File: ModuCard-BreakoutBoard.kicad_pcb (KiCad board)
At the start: 2 copper layers, 41 parts, among them J1 09031967921, J10 USB_C_Receptacle_USB2.0_16P, J9 RJ45_LED_Shielded, Q1 AO3401A, Q2 AO3401A, SW1 SW_SPDT_321, SW2 SW_SPDT_321, SW3 SW_SPDT_321, U1 XL4015, U2 IP4234CZ6,115

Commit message: Create fundamental layout
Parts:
- added J11: Barrel_Jack_Switch, Connector_BarrelJack:BarrelJack_Kycon_KLDX-0202-xC_Horizontal, F.Cu at (31.2, 78.5)
- added J3: Conn_01x16_Pin, Connector_PinHeader_2.54mm:PinHeader_1x16_P2.54mm_Vertical, F.Cu at (25.1, 113.0)
- added J4: Conn_01x16_Pin, Connector_PinHeader_2.54mm:PinHeader_1x16_P2.54mm_Vertical, F.Cu at (36.0, 63.9)
- added J5: Conn_01x16_Pin, Connector_PinHeader_2.54mm:PinHeader_1x16_P2.54mm_Vertical, F.Cu at (54.0, 64.0)
- added J6: Barrel_Jack_Switch, Connector_BarrelJack:BarrelJack_Kycon_KLDX-0202-xC_Horizontal, F.Cu at (30.5, 58.5)
- added J7: Conn_01x02_Pin, Connector_PinHeader_2.54mm:PinHeader_1x02_P2.54mm_Vertical, F.Cu at (52.9, 30.5)
- added J8: Conn_01x02_Pin, Connector_PinHeader_2.54mm:PinHeader_1x02_P2.54mm_Vertical, F.Cu at (52.9, 36.7)
- L1: value 4.7uH,25mA -> 40uH; footprint PCM_JLCPCB:L_1206 -> Inductor_SMD:L_Bourns_SRR1260
- moved U2 67.3 mm to (53.0, 23.0), turned to -90 degrees
- moved R9 62.3 mm to (54.8, 20.3), turned to 180 degrees
- moved J10 61.9 mm to (60.5, 23.0), turned to 90 degrees
- moved H3 61.2 mm to (70.5, 14.0)
- moved C8 60.4 mm to (57.1, 17.1), turned to 180 degrees
- moved H2 59.0 mm to (14.5, 113.0)
- moved R10 58.8 mm to (54.7, 25.6), turned to 180 degrees
- moved H4 54.6 mm to (68.5, 113.5)
- moved R8 52.4 mm to (56.9, 28.9), turned to 180 degrees
- moved C9 52.4 mm to (54.7, 26.6), turned to 180 degrees
- moved H1 42.8 mm to (14.5, 14.0)
- moved D2 41.1 mm to (22.0, 24.0), turned to 180 degrees
- moved SW2 40.3 mm to (25.2, 69.0)
- moved D5 40.1 mm to (24.0, 14.0)
- moved Q1 37.3 mm to (34.6, 60.0), turned to 180 degrees
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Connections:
- R5 pad 2: +12V_DC_JACK -> +12V
- R6 pad 2: +12V_DC_JACK -> +12V
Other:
- board outline added: 54 x 101 mm

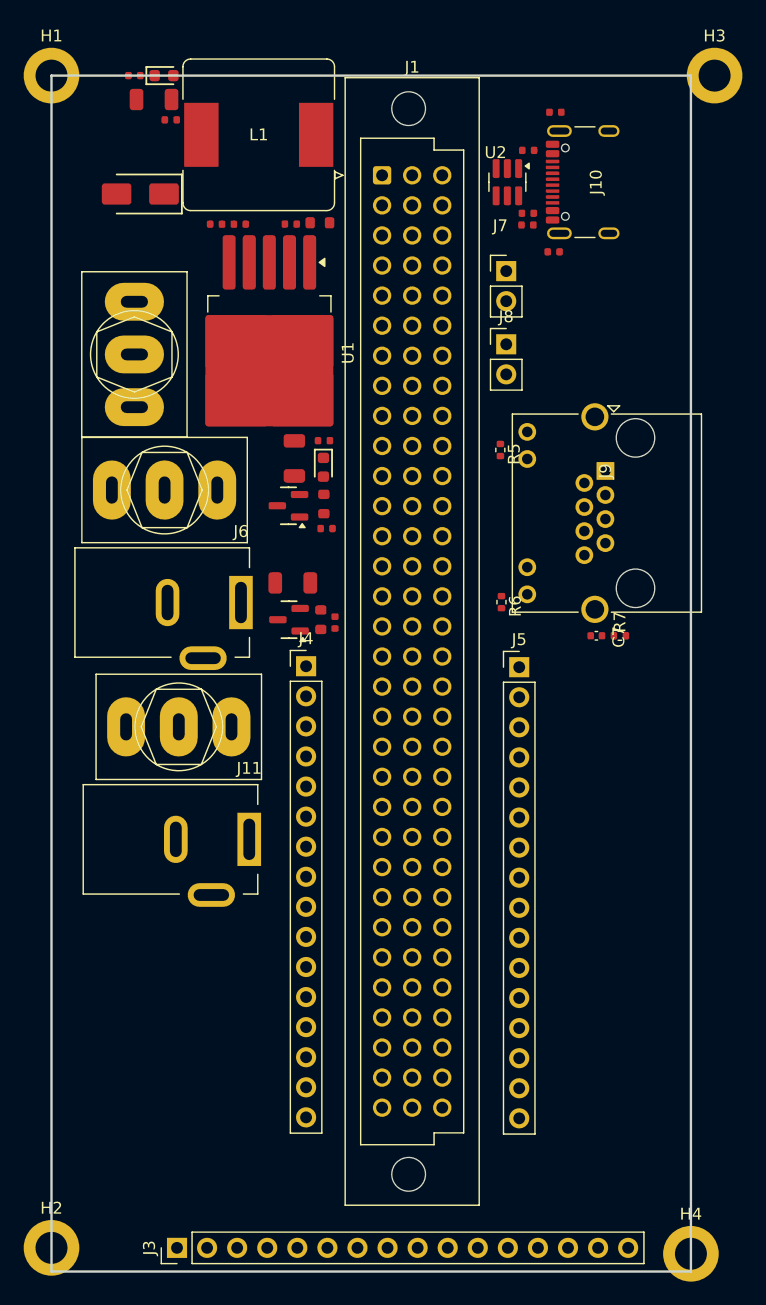
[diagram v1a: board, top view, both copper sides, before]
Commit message: Fix converter placement
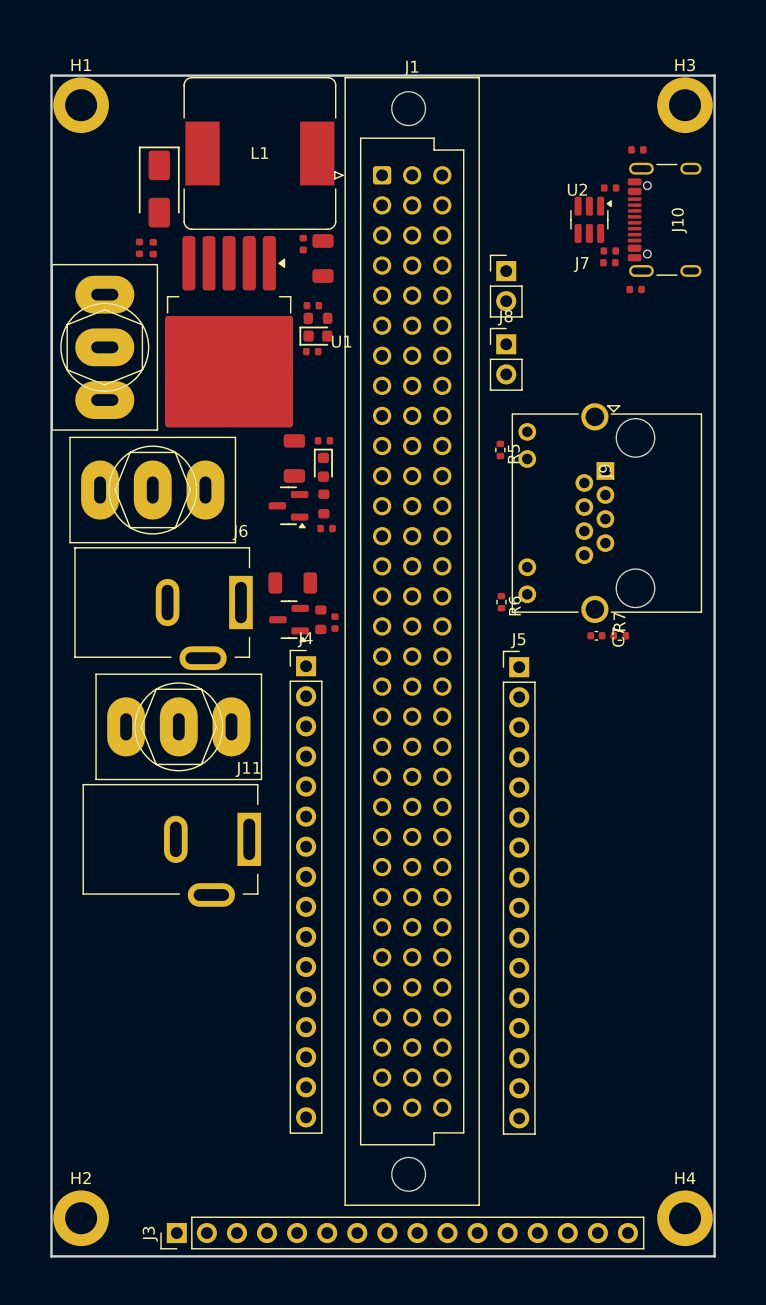
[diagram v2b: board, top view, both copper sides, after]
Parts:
- moved R4 27.7 mm to (36.5, 37.3), turned to 0 degrees
- moved D5 25.6 mm to (37.0, 36.0)
- moved C5 19.6 mm to (37.4, 29.4), turned to -90 degrees
- moved C4 15.3 mm to (35.8, 28.2), turned to -90 degrees
- moved R1 8.07 mm to (37.0, 34.5), turned to 180 degrees
- moved C8 7.62 mm to (64.0, 20.3)
- moved C9 7.62 mm to (61.6, 29.8)
- moved R10 7.62 mm to (61.6, 28.8)
- moved R8 7.62 mm to (63.8, 32.1)
- moved J10 7.62 mm to (67.4, 26.2)
- moved R9 7.62 mm to (61.7, 23.5)
- moved U2 7.62 mm to (59.9, 26.2)
- moved C1 7.58 mm to (23.1, 28.6), turned to 90 degrees
- moved R2 7.13 mm to (36.6, 33.4), turned to 0 degrees
- moved C3 6.77 mm to (21.9, 28.6), turned to 90 degrees
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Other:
- board size 54 x 101 mm -> 56 x 99.7 mm

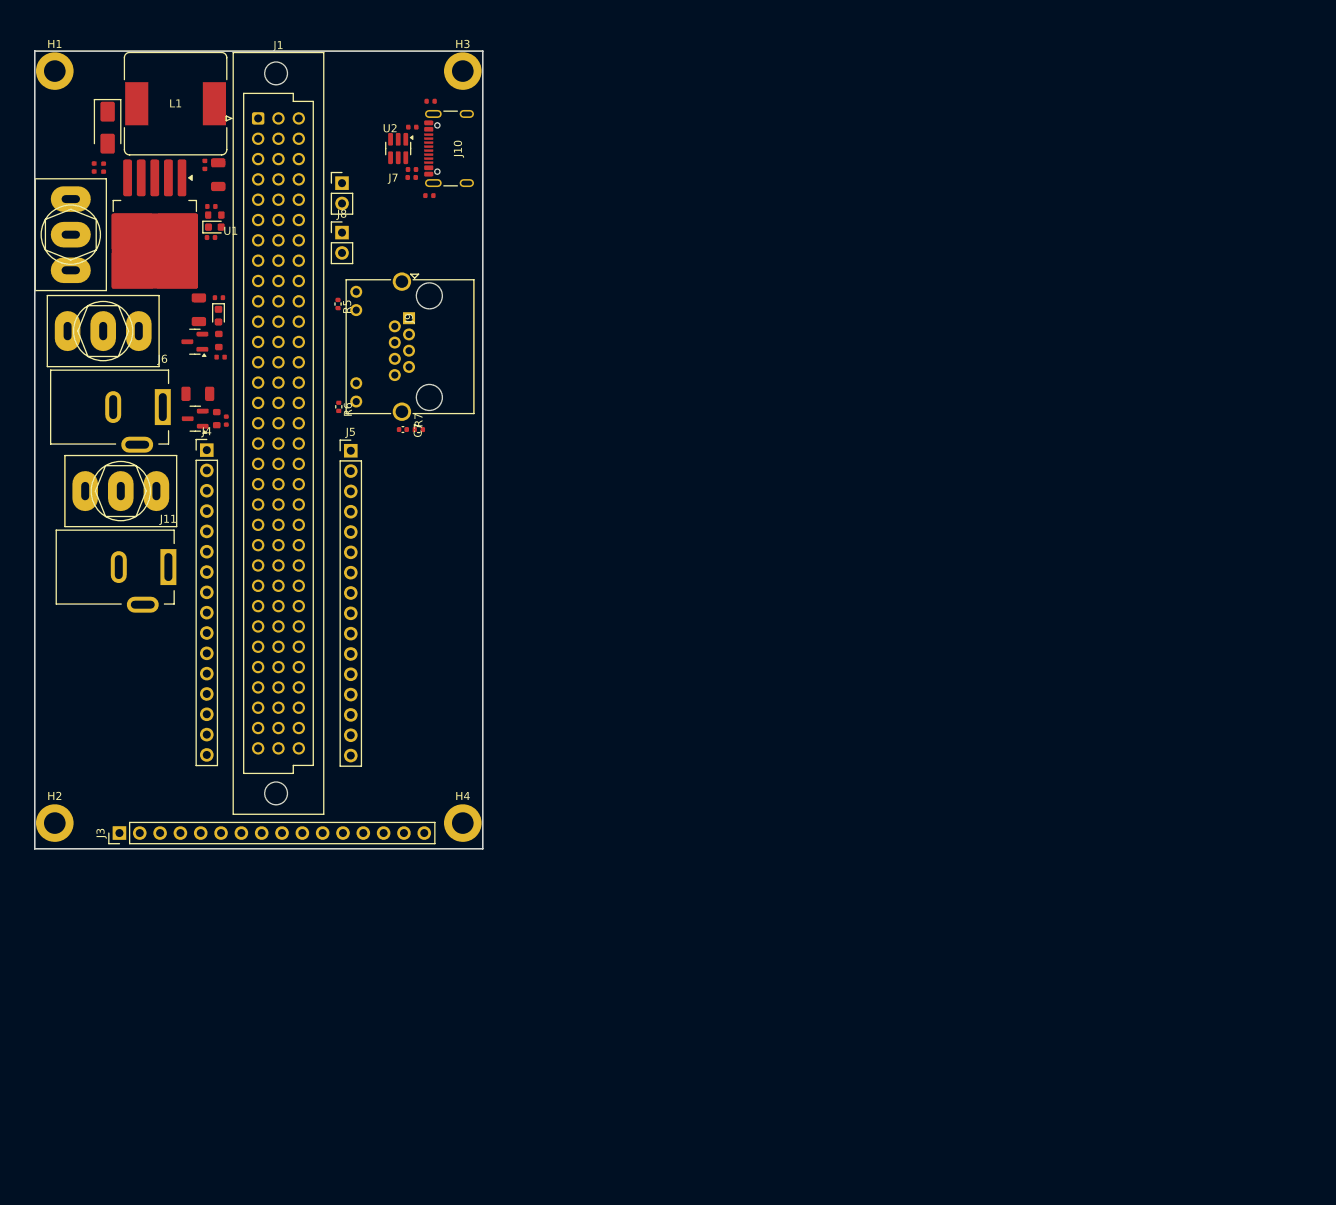
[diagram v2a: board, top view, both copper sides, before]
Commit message: Change PCB size
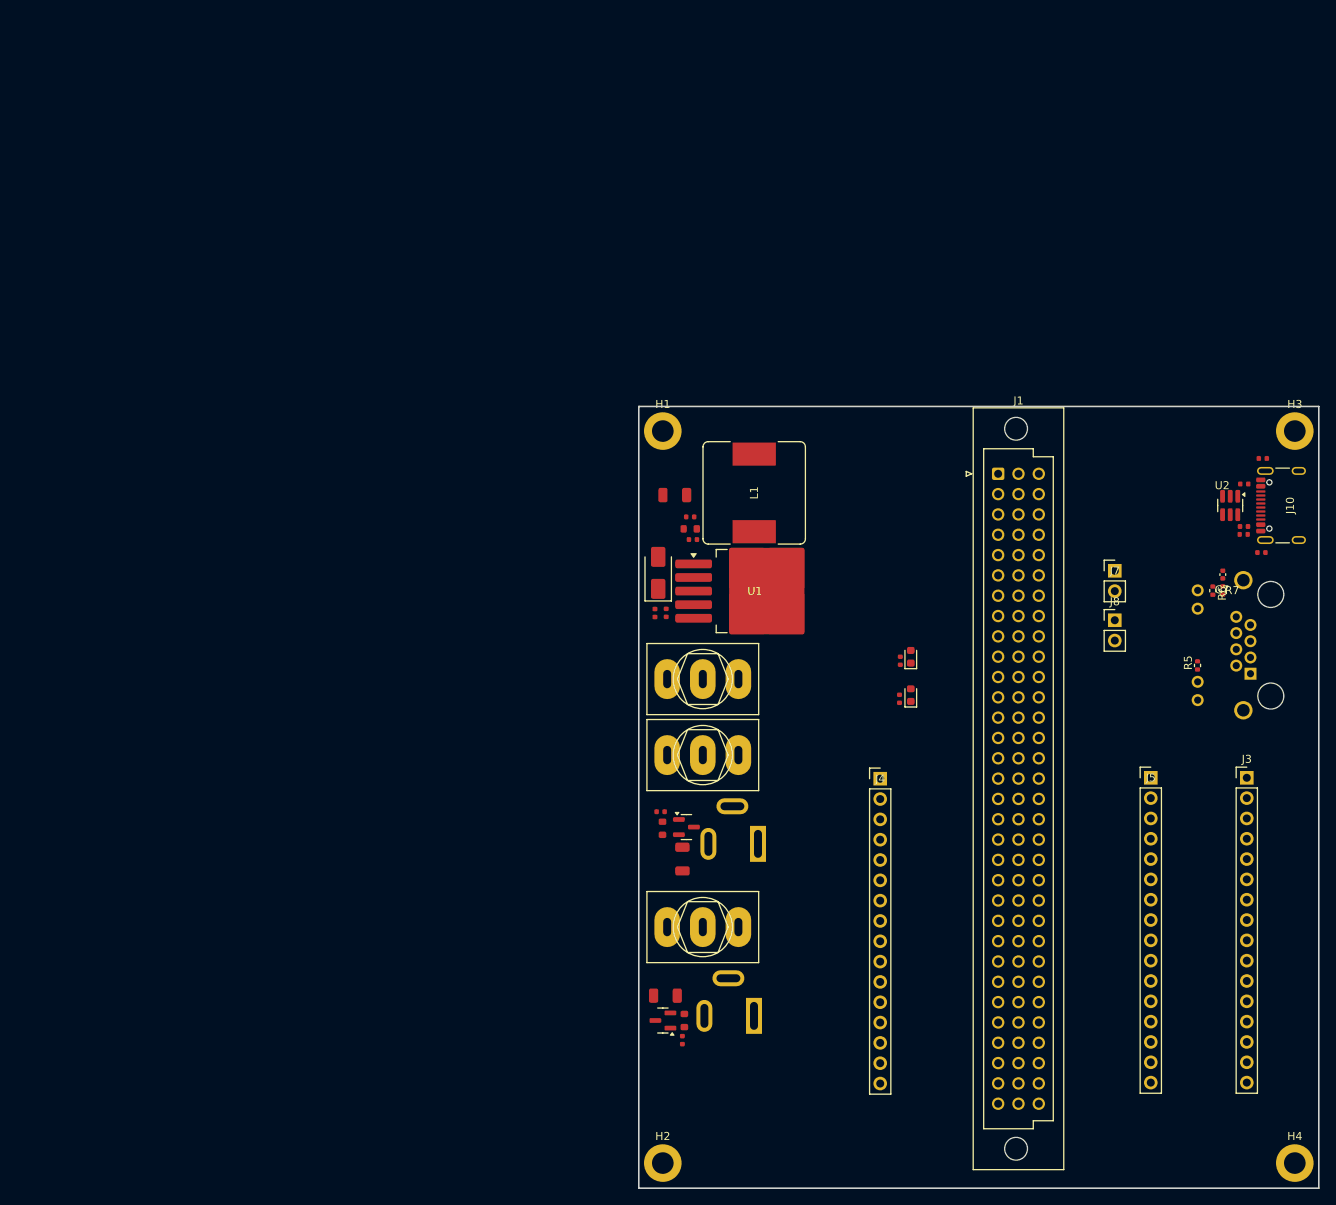
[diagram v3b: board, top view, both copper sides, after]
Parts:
- J11, J6, J9: moved to B.Cu
- moved J3 141.1 mm to (166.0, 104.8), turned to 0 degrees
- moved R5 116.5 mm to (159.8, 90.8), turned to 90 degrees
- moved J9 114.2 mm to (166.5, 91.8), turned to 90 degrees
- moved H3 113.3 mm to (172.0, 61.5)
- moved C8 113.2 mm to (168.0, 64.9)
- moved J10 113.2 mm to (171.4, 70.8)
- moved R9 113.2 mm to (165.7, 68.1)
- moved U2 113.2 mm to (163.9, 70.8)
- moved R10 113.2 mm to (165.6, 73.4)
- moved R8 113.2 mm to (167.8, 76.7)
- moved C9 113.2 mm to (165.6, 74.4)
- moved H4 112.3 mm to (172.0, 153.0)
- moved R6 111.6 mm to (161.7, 81.4)
- moved J7 108.1 mm to (149.5, 79.0)
- moved J8 108.1 mm to (149.5, 85.1)
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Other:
- board size 56 x 99.7 mm -> 85 x 97.7 mm

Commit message: Finish layout
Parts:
- added R15: 120Ω, PCM_JLCPCB:R_1206, F.Cu at (115.5, 81.4)
- added R16: 120Ω, PCM_JLCPCB:R_1206, F.Cu at (115.5, 83.9)
- added R17: 10kΩ, PCM_JLCPCB:R_0603, F.Cu at (157.5, 65.5)
- added R18: 22kΩ, PCM_JLCPCB:R_0402, F.Cu at (156.0, 65.8)
- added S1: DIP Switch x 2, PCM_JLCPCB:SW-SMD_218-2LPSTRF, F.Cu at (122.5, 82.9)
- added U4: TS3USB30EDGSR, Package_SO:VSSOP-10_3x3mm_P0.5mm, F.Cu at (156.5, 70.5)
- added U5: AMS1117-3.3, Package_TO_SOT_SMD:SOT-223-3_TabPin2, F.Cu at (157.2, 79.0)
- moved C7 3.88 mm to (163.0, 83.3)
- moved J9 3.88 mm to (166.5, 95.7)
- moved R5 3.88 mm to (159.8, 94.7)
- moved R6 3.88 mm to (161.7, 85.3)
- moved R7 3.88 mm to (163.0, 85.3)
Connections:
- J1 pad a2: /DIN41612_breakout/USB.+ -> /DIN41612_breakout/USB_DIN.+
- J1 pad c2: /DIN41612_breakout/USB.- -> /DIN41612_breakout/USB_DIN.-
- J9 pad 7: /DIN41612_breakout/USB.- -> /RJ45/USB_RJ.-
- J9 pad 8: /DIN41612_breakout/USB.+ -> /RJ45/USB_RJ.+
- U2 pad 3: /DIN41612_breakout/USB.+ -> /USB/USB_port.+
- U2 pad 4: /DIN41612_breakout/USB.- -> /USB/USB_port.-
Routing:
- net /USB/USB_port.-: track 0.00 -> 7.98 mm
- net /USB/USB_port.+: track 0.00 -> 7.48 mm

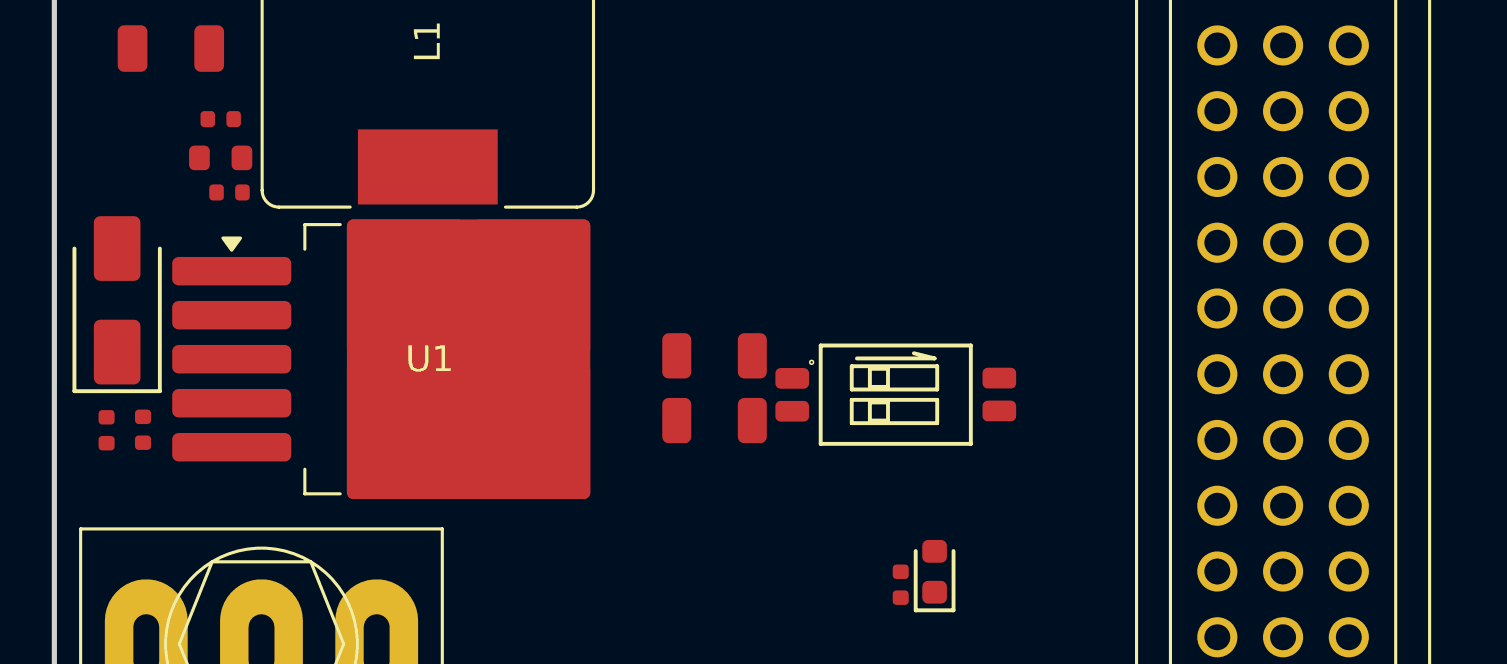
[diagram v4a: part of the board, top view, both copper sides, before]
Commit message: Change DRC rules
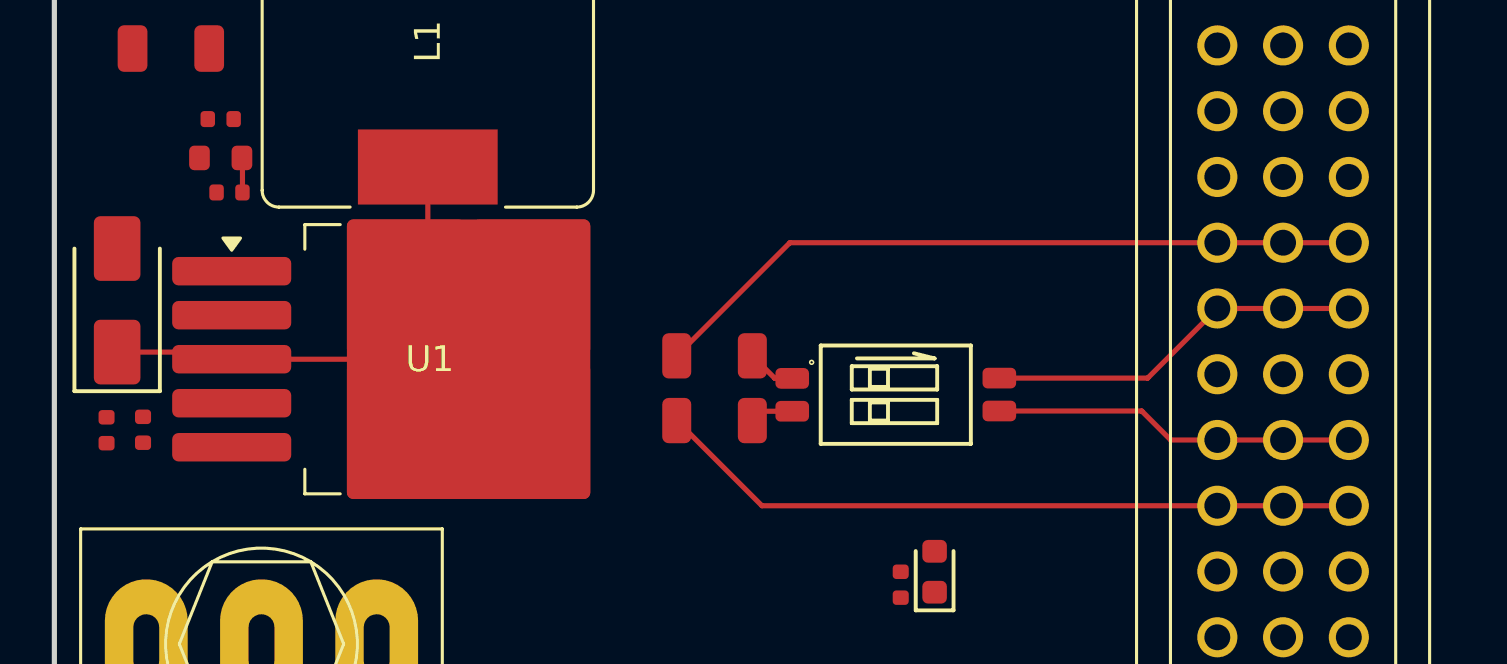
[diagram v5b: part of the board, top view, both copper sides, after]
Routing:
- net /Connector/CAN1.+: track 0.00 -> 27.8 mm
- net /Connector/CAN2.-: track 0.00 -> 27.3 mm
- net Net-(U1-SW): track 0.00 -> 18.7 mm
- net /Connector/CAN1.-: track 0.00 -> 14.6 mm
- net /Connector/CAN2.+: track 0.00 -> 14.0 mm
- net Net-(R15-Pad1): track 0.00 -> 1.90 mm
- net Net-(R16-Pad1): track 0.00 -> 1.69 mm
- net Net-(U1-FB): track 0.00 -> 1.34 mm
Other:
- copper layers 2 -> 4
- rule pad_to_mask_clearance: 0 -> 0.038

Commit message: Make paths
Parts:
- moved R5 2.99 mm to (162.0, 96.8), turned to 0 degrees
- moved R17 0.75 mm to (157.5, 64.8)
- moved R18 0.75 mm to (156.0, 65.0)
- moved R9 0.44 mm to (165.2, 68.1)
- moved C7 0.25 mm to (163.2, 83.3)
- moved R7 0.25 mm to (163.2, 85.3)
- moved R6 0.25 mm to (161.5, 85.3)
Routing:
- net /Connector/CAN2.+: track 14.0 -> 55.4 mm
- net /Connector/CAN1.-: track 14.6 -> 49.6 mm
- net /Connector/CAN1.+: track 27.8 -> 62.1 mm
- net /RJ45/USB_RJ.+: track 0.00 -> 31.3 mm, vias 0 -> 2
- net Net-(C7-Pad1): track 0.00 -> 30.4 mm
- net /Connector/GPIOC0: track 0.00 -> 30.4 mm
- net /Connector/GPIOC8: track 0.00 -> 29.7 mm
- net /Connector/GPIOC6: track 0.00 -> 29.7 mm
- net /Connector/GPIOC9: track 0.00 -> 29.7 mm
- net /Connector/GPIOC13: track 0.00 -> 29.7 mm
- net /Connector/GPIOC4: track 0.00 -> 29.6 mm
- net /Connector/GPIOC3: track 0.00 -> 29.6 mm
- net /Connector/GPIOC12: track 0.00 -> 29.6 mm
- net /Connector/GPIOC7: track 0.00 -> 29.6 mm
- net /Connector/GPIOC10: track 0.00 -> 29.6 mm
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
